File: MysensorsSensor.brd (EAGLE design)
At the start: 26.2 x 44.1 mm, 41 parts, among them IC1 APE8865Y5-30-HF-3, IC2 AT25DF512C-SSHN-B, IC3 ATSHA204A, IC4 MCP1640CT-I/CHY, IC5 ATMEGA328P-AU

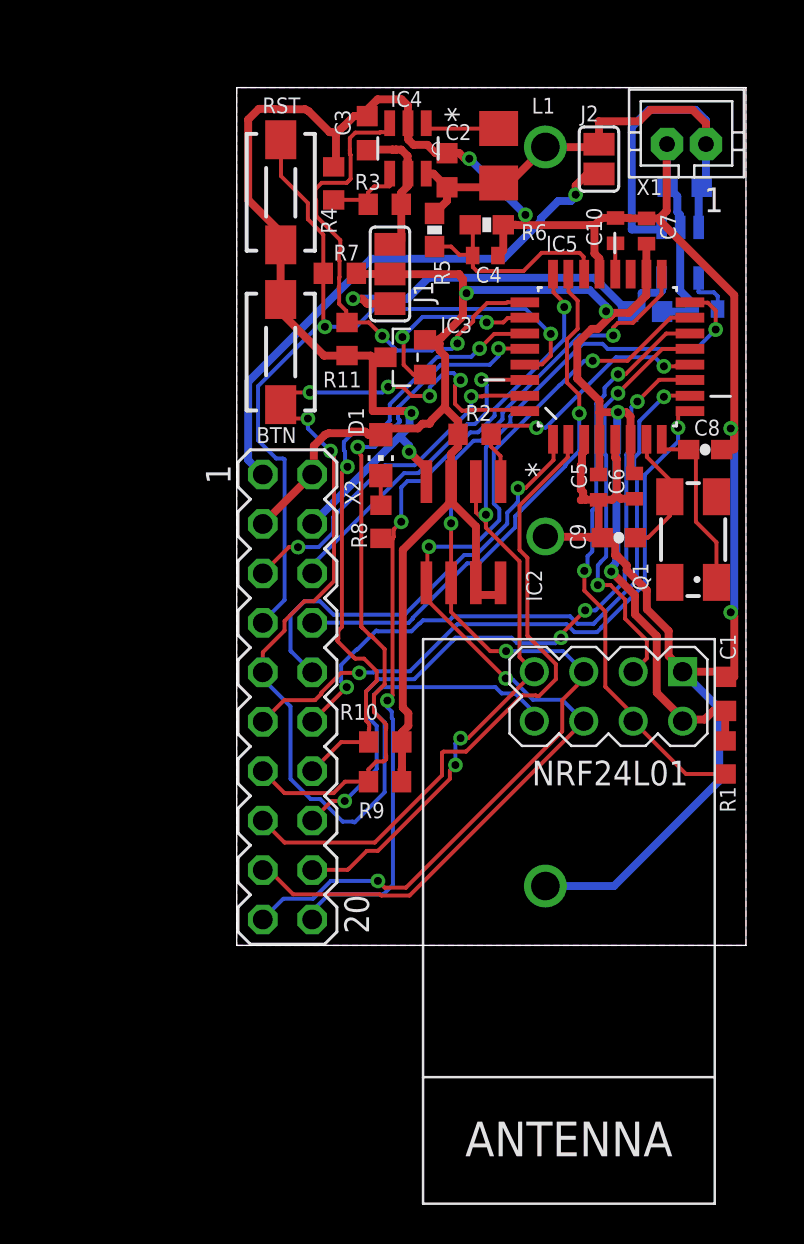
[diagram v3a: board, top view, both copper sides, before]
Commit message: use p-mosfet for reverse polarity
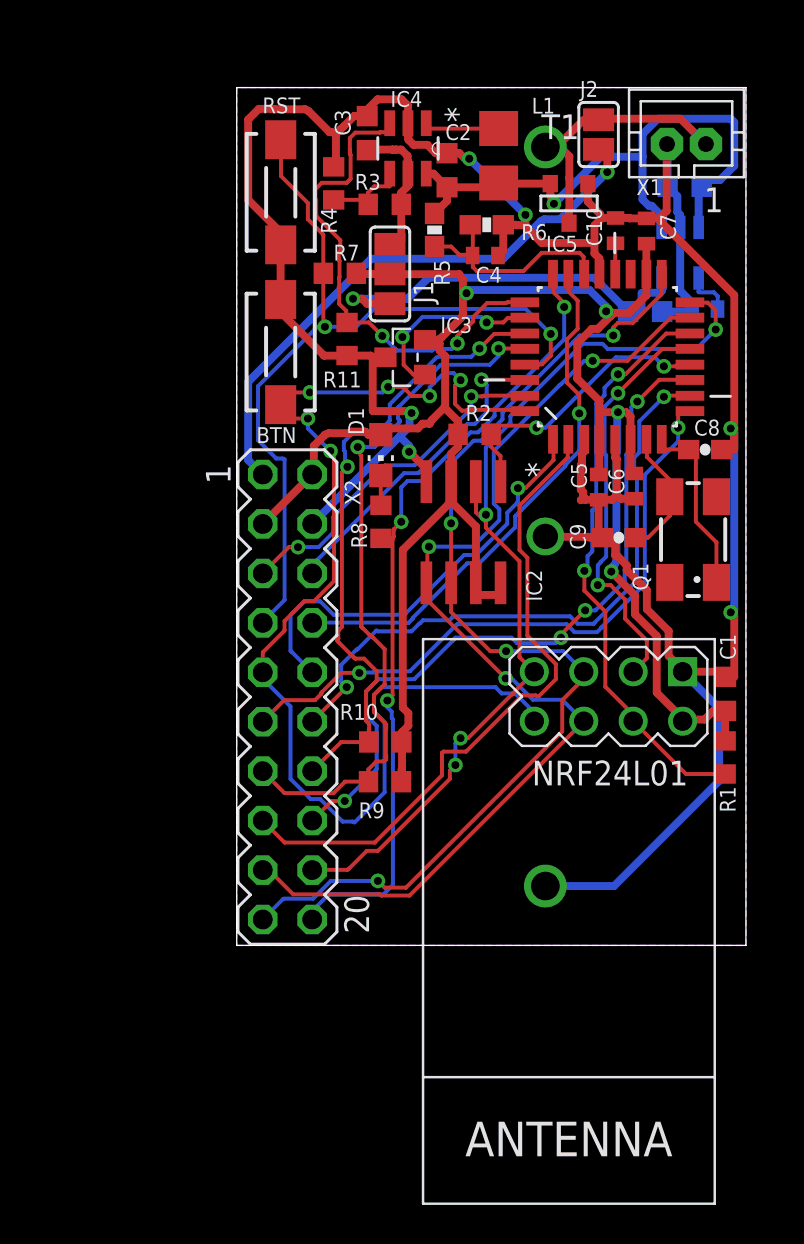
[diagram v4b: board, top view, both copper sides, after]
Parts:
- added T1: (no value), zetex:SOT-23
- moved J2 1.26 mm to (18.6, 41.7)
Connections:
- net N$5 renamed VRAW
- new net N$7: CR123A.+, CR2032.1, J2.1, T1.1, X1.1
- net GND: now also T1.3
- net VBAT: now also T1.2; no longer CR123A.+, CR2032.1, J2.1, X1.1
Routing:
- net N$7: track 0.00 -> 13.6 mm
- net VBAT: track 36.9 -> 32.3 mm, vias 0 -> 1
- net GND: track 152.0 -> 154.8 mm
- net VRAW: track 27.9 -> 29.6 mm

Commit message: add RFM69
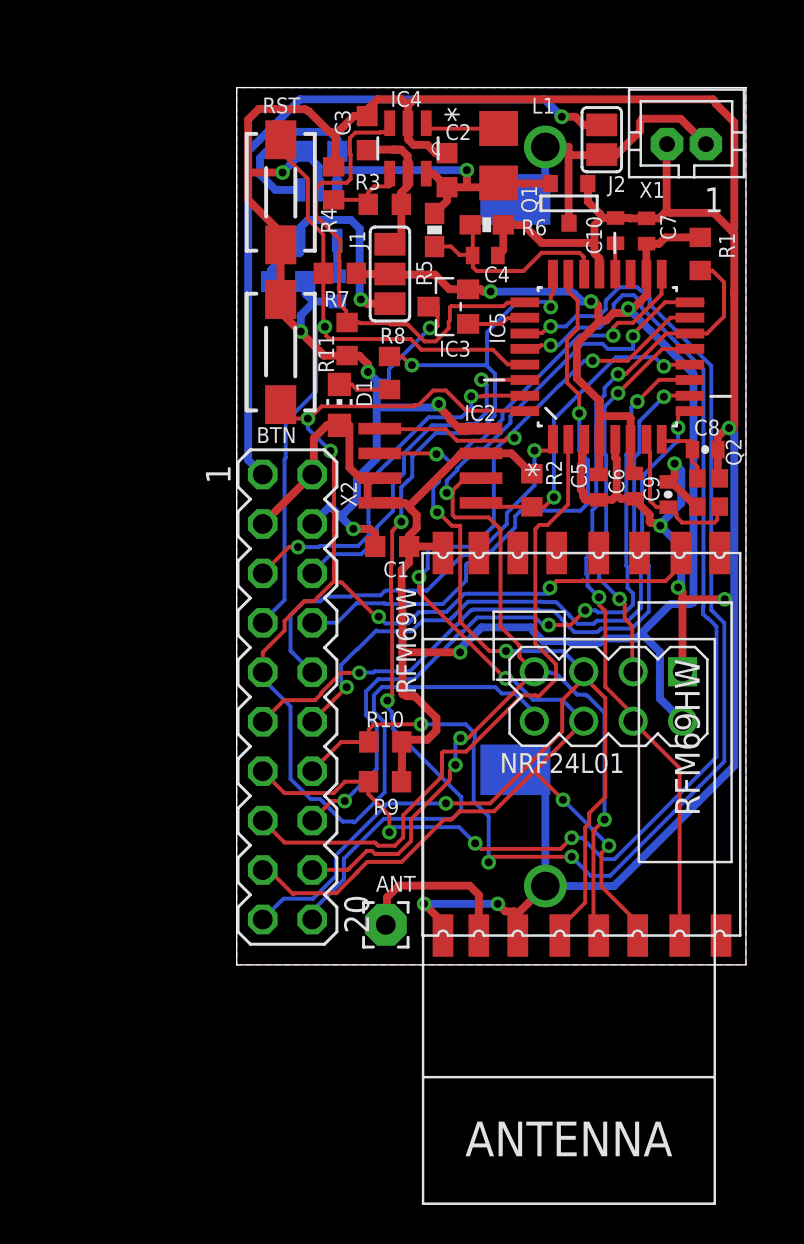
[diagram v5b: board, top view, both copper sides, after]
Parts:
- removed T1: (no value), zetex:SOT-23
- added ANT: WIREPAD2,15/1,0, wirepad:2,15/1,0
- added Q2: FA-128, crystal:FA-128
- added RFM69W: RFM69HW, hoperf:RFM
- C8, C9: device SparkFun-Passives:0603-CAP -> SparkFun-Passives:0402-CAP
- CR2032: value 3V -> (none); device SparkFun-Batteries:BATTCOM_20MM_PTH -> Wurth_Elektronik_Electromechanic_Assembly_Spacer_rev15d:79527141
- Q1: device crystal:CTS406 -> zetex:SOT-23
- moved R1 25.9 mm to (23.8, 35.5)
- moved C12 18.9 mm to (5.17, 33.7), turned to 90 degrees
- moved C14 18.8 mm to (4.30, 40.8)
- moved C1 18.7 mm to (7.99, 20.5), turned to 0 degrees
- moved IC1 18.7 mm to (4.21, 37.5)
- moved Q1 18.4 mm to (17.0, 38.1), turned to 0 degrees
- moved C13 18.4 mm to (2.65, 34.1)
- moved R8 7.66 mm to (7.85, 29.4), turned to 90 degrees
- moved CR2032 5.70 mm to (14.3, 23.7)
- moved R2 4.11 mm to (15.2, 23.4), turned to 90 degrees
- moved IC2 3.81 mm to (9.95, 24.6), turned to 90 degrees
- moved IC3 3.42 mm to (10.9, 32.8)
- moved C9 3.36 mm to (22.2, 23.2), turned to 270 degrees
- moved D1 3.34 mm to (5.28, 27.8), turned to 0 degrees
- moved J2 0.31 mm to (18.8, 41.4), turned to 90 degrees
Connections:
- new net N$5: ANT.1, RFM69W.ANT
- net D10: now also RFM69W.NSS
- net D2: now also RFM69W.DIO0
- net GND: now also CR2032.-, Q1.3, Q2.2, Q2.4, RFM69W.GNDA, RFM69W.GNDB; no longer CR2032.2, T1.3
- net MISO: now also RFM69W.MISO
- net MOSI: now also RFM69W.MOSI
- net N$2: now also Q2.3; no longer Q1.1
- net N$6: now also Q2.1; no longer Q1.3
- net N$7: now also CR2032.+, Q1.1; no longer CR2032.1, T1.1
- net SCK: now also RFM69W.SCK
- net VBAT: now also Q1.2; no longer T1.2
- net VCC: now also RFM69W.VCC
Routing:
- net GND: track 154.8 -> 203.8 mm, vias 6 -> 13
- net A4: track 32.8 -> 65.4 mm, vias 2 -> 4
- net A5: track 36.6 -> 62.0 mm, vias 2 -> 4
- net SCK: track 54.8 -> 75.3 mm, vias 4 -> 5
- net MOSI: track 55.7 -> 74.2 mm, vias 3 -> 6
- net MISO: track 48.5 -> 66.2 mm, vias 4 -> 5
- net D2: track 60.7 -> 78.2 mm, vias 6 -> 4
- net VCC: track 104.2 -> 119.6 mm
- net D10: track 30.0 -> 41.4 mm
- net A1: track 42.3 -> 52.1 mm, vias 3 -> 4
- net N$5: track 0.00 -> 8.68 mm
- net VREG: track 20.7 -> 12.4 mm
- net VRAW: track 29.6 -> 36.7 mm
- net A3: track 9.69 -> 3.05 mm, vias 2 -> 0
- net N$2: track 9.54 -> 3.69 mm
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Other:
- board size 26.2 x 44.1 mm -> 26.2 x 45.1 mm
- board text added: "MySensors 1.3"
- board text removed: "MySensors 1.2"

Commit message: add 0Ohm resistor for radio module interrupt + connect button to D3
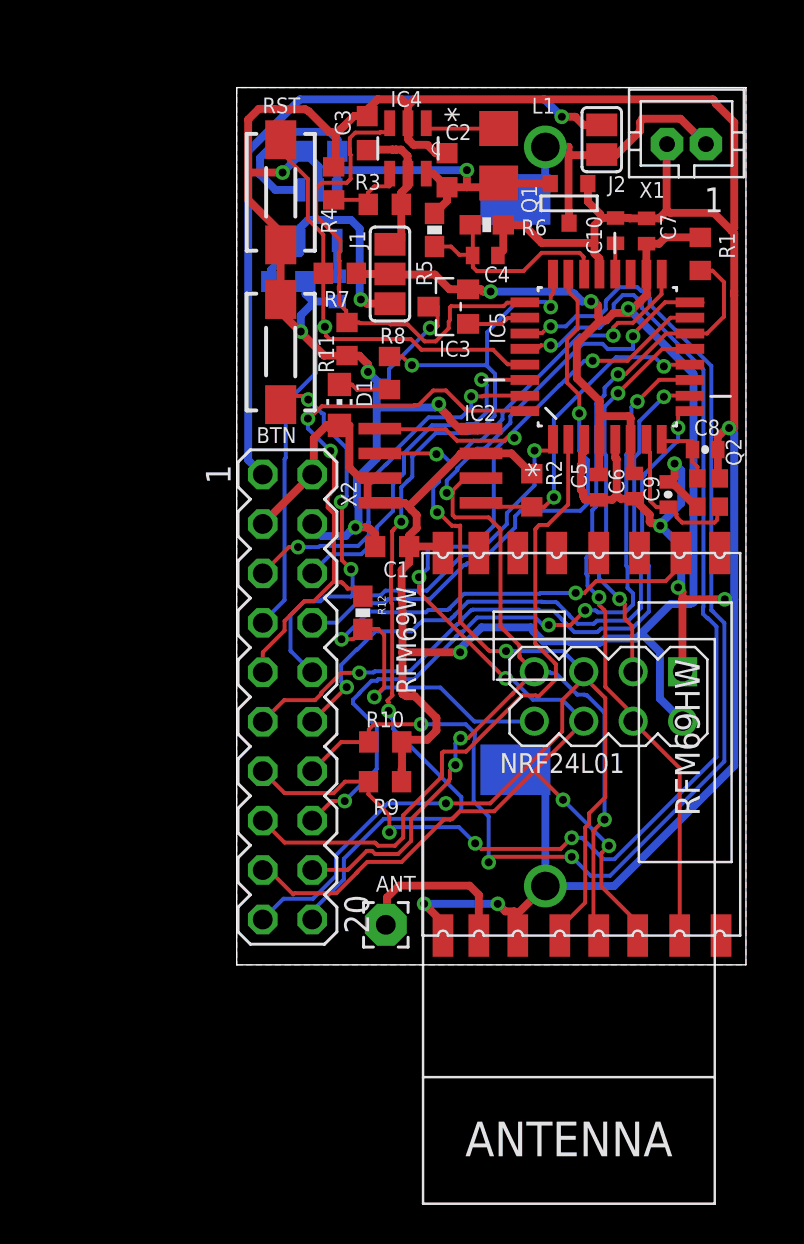
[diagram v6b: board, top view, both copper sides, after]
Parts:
- added R12: 0, SparkFun-Passives:0603-RES
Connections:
- new net N$9: NRF24L01.8, R12.2, RFM69W.DIO0
- net D2: now also R12.1; no longer BTN.2, NRF24L01.8, RFM69W.DIO0
- net D3: now also BTN.2
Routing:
- net D2: track 78.2 -> 30.1 mm, vias 4 -> 2
- net N$9: track 0.00 -> 35.3 mm, vias 0 -> 3
- net D3: track 22.3 -> 35.5 mm, vias 1 -> 4
- net D7: track 38.6 -> 39.3 mm
- net A0: track 30.3 -> 29.8 mm

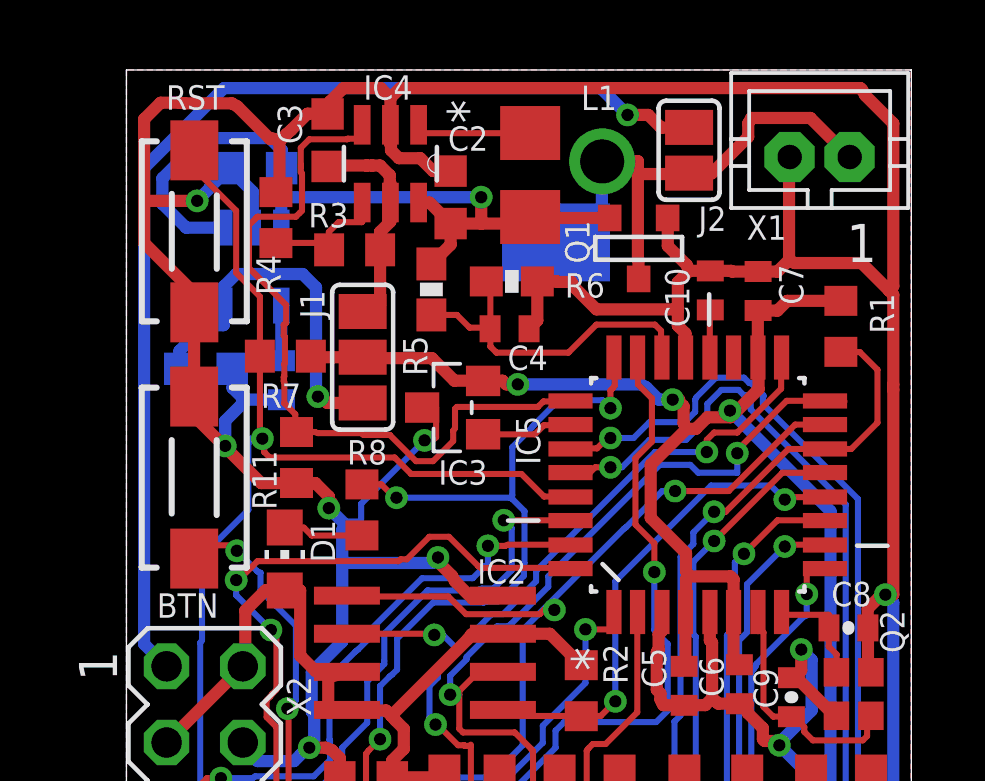
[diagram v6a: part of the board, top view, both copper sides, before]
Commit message: move ldo to top layer
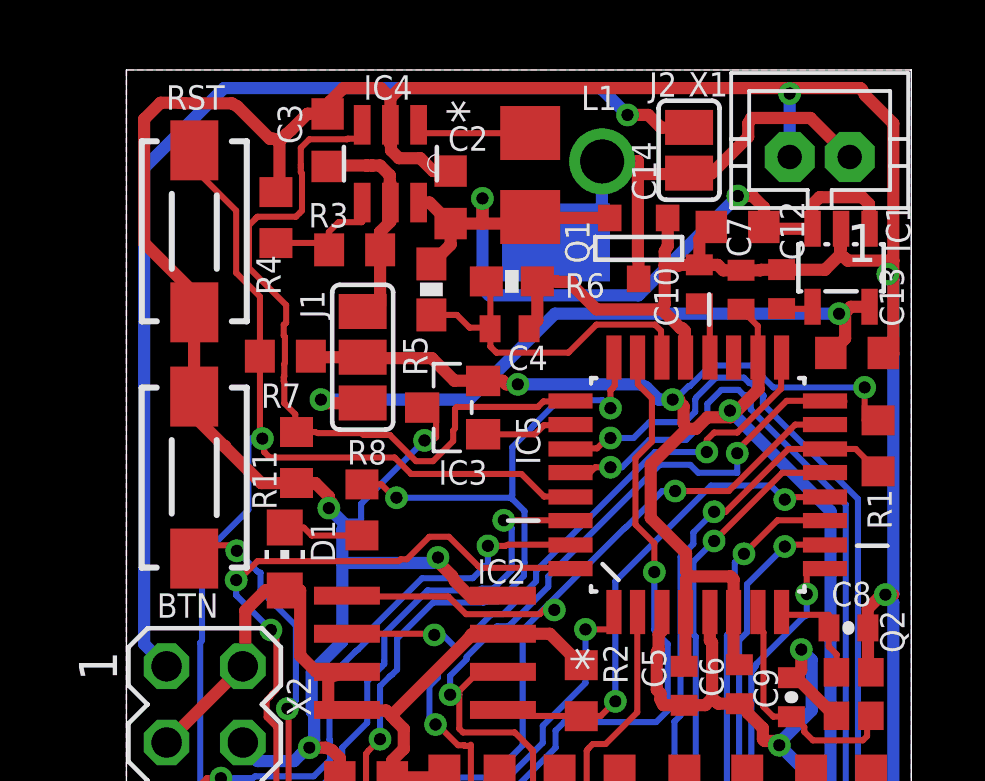
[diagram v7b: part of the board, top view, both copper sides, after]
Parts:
- moved C13 21.7 mm to (24.4, 34.6), flipped to the top, turned to 0 degrees
- moved IC1 19.6 mm to (23.8, 37.5), flipped to the top
- moved C12 16.9 mm to (21.8, 36.8), flipped to the top, turned to 270 degrees
- moved C14 16.2 mm to (20.4, 38.8), flipped to the top, turned to 180 degrees
- moved R1 4.17 mm to (25.1, 31.5)
- moved C7 0.57 mm to (20.5, 36.7)
- moved C10 0.42 mm to (19.1, 36.9)
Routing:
- net VREG: track 12.4 -> 22.5 mm, vias 1 -> 2
- net VCC: track 119.6 -> 125.6 mm, vias 4 -> 5
- net GND: track 203.7 -> 198.3 mm
- net D10: track 41.4 -> 38.1 mm
- net VBAT: track 26.5 -> 29.3 mm, vias 1 -> 2
- net N$8: track 1.84 -> 1.10 mm

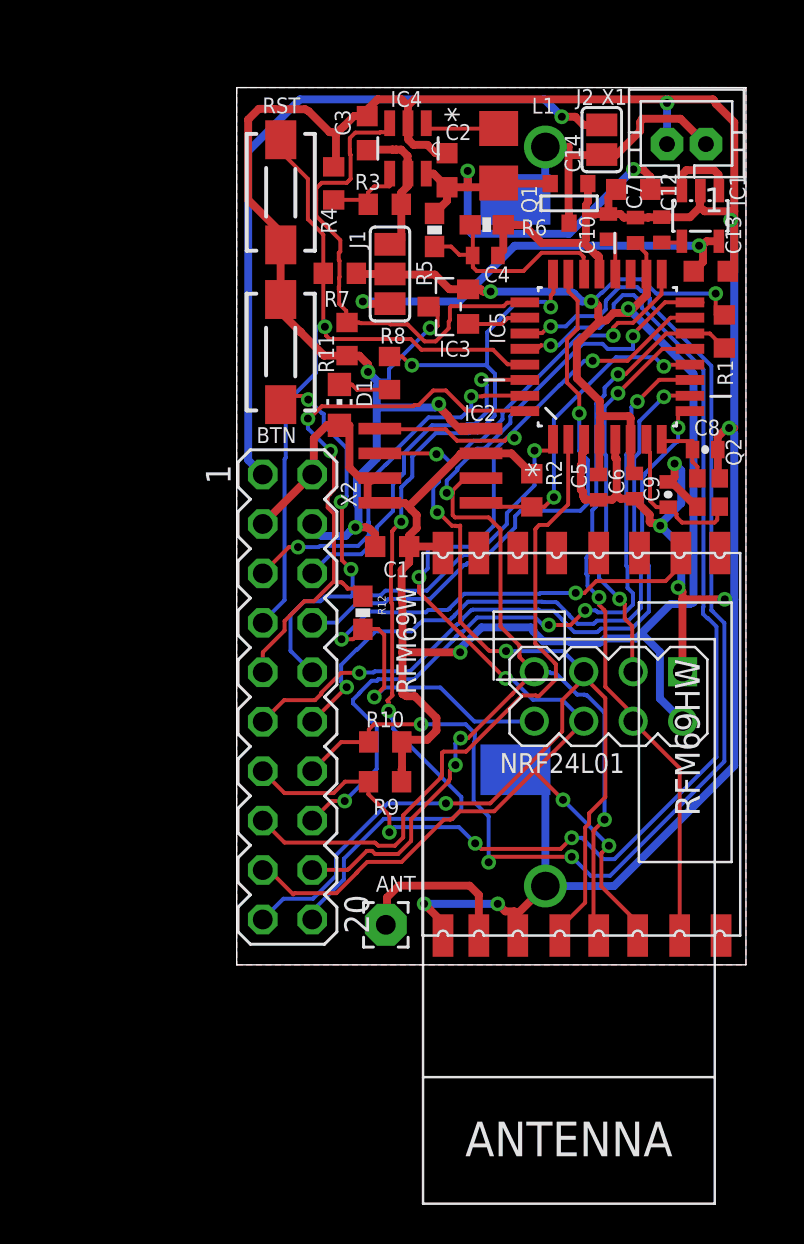
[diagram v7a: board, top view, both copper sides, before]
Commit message: rotate cr2032 battery pack to about 55 degrees
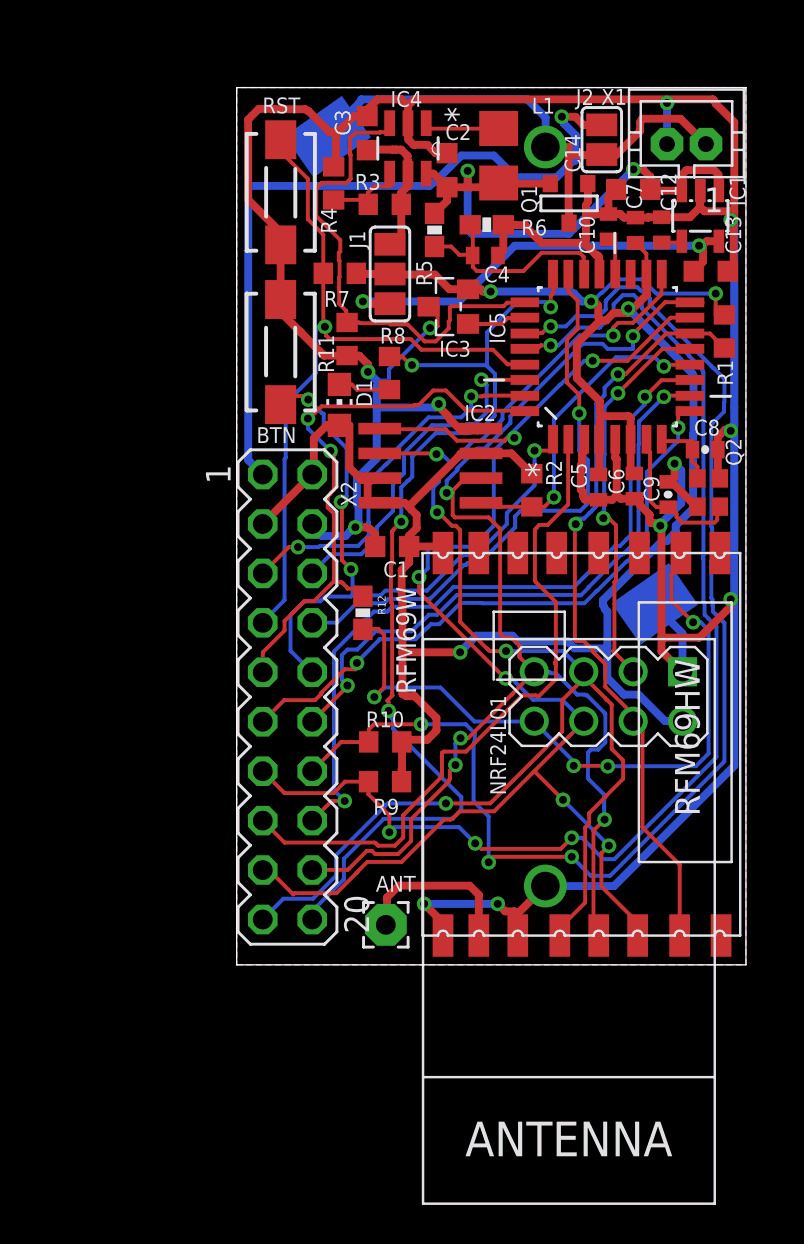
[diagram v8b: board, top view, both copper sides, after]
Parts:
- moved CR2032 6.00 mm to (13.1, 29.5), turned to 55 degrees
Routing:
- net N$7: track 17.5 -> 27.8 mm
- net D5: track 35.0 -> 31.8 mm
- net D6: track 34.3 -> 31.2 mm
- net GND: track 198.3 -> 196.6 mm, vias 13 -> 12
- net D7: track 39.3 -> 37.8 mm, vias 4 -> 2
- net N$9: track 35.3 -> 36.7 mm, vias 3 -> 4
- net VRAW: track 36.7 -> 38.2 mm
- net MISO: track 66.2 -> 67.4 mm
- net D10: track 38.1 -> 39.2 mm
- net SCK: track 75.3 -> 75.9 mm
- net A4: track 65.4 -> 66.0 mm
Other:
- board text added: "1.3 MySensors"
- board text removed: "MySensors 1.3"
